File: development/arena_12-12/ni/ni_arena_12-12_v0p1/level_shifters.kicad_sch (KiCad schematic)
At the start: 15 parts, among them U1 TXB0108PW, U2 TXB0108PW, U3 TXB0108PW, U4 TXB0108PW, U5 TXB0108PW

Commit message: Further work on 12-12 ni arena.
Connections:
- net PAN3V.EXT_INT: now also U5.8 (A7); no longer U4.8 (A7)
- net PAN3V.RESET: now also U5.9 (A8); no longer U4.9 (A8)
- net PAN5V.EXT_INT: now also U5.13 (B7); no longer U4.13 (B7)
- net PAN5V.RESET: now also U5.12 (B8); no longer U4.12 (B8)
- net PAN3V.CS_00: now reaches U1.1 (A1)
- net PAN5V.CS_00: now reaches U1.20 (B1)
- net PAN3V.MOSI_09: now reaches U5.1 (A1)
- net PAN5V.MISO_11: now reaches U5.14 (B6)
- net PAN5V.MOSI_11: now reaches U5.15 (B5)
- net PAN5V.MISO_10: now reaches U5.16 (B4)
- net PAN5V.MOSI_10: now reaches U5.17 (B3)
- net PAN5V.MISO_09: now reaches U5.18 (B2)
- net PAN5V.MOSI_09: now reaches U5.20 (B1)
- net PAN3V.MISO_09: now reaches U5.3 (A2)
- net PAN3V.MOSI_10: now reaches U5.4 (A3)
- net PAN3V.MISO_10: now reaches U5.5 (A4)
- net PAN3V.MOSI_11: now reaches U5.6 (A5)
- net PAN3V.MISO_11: now reaches U5.7 (A6)
- net PAN3V.SCK_00: now reaches U2.1 (A1)
- net PAN5V.SCK_00: now reaches U2.20 (B1)
- net PAN3V.MOSI_01: now reaches U3.1 (A1)
- net PAN5V.MOSI_01: now reaches U3.20 (B1)
- net PAN3V.MOSI_05: now reaches U4.1 (A1)
- net PAN5V.MOSI_05: now reaches U4.20 (B1)
- net PAN3V.CS_0 renamed PAN3V.CS_01
- net PAN3V.CS_1 renamed PAN3V.CS_02
- net PAN3V.CS_2 renamed PAN3V.CS_03
- net PAN3V.CS_3 renamed PAN3V.CS_04
- net PAN3V.CS_4 renamed PAN3V.CS_05
- net PAN3V.CS_5 renamed PAN3V.CS_06
- net PAN3V.CS_6 renamed PAN3V.CS_07
- net PAN3V.CS_7 renamed PAN3V.SCK_01
- net PAN3V.MISO_0 renamed PAN3V.MOSI_02
- net PAN3V.MISO_1 renamed PAN3V.MOSI_03
- net PAN3V.MISO_2 renamed PAN3V.MOSI_04
- net PAN3V.MISO_3 renamed PAN3V.MISO_05
- net PAN3V.MISO_4 renamed PAN3V.MISO_06
- net PAN3V.MISO_5 renamed PAN3V.MISO_07
- net PAN3V.MOSI_0 renamed PAN3V.MISO_01
- net PAN3V.MOSI_1 renamed PAN3V.MISO_02
- net PAN3V.MOSI_2 renamed PAN3V.MISO_03
- net PAN3V.MOSI_3 renamed PAN3V.MISO_04
- net PAN3V.MOSI_4 renamed PAN3V.MOSI_06
- net PAN3V.MOSI_5 renamed PAN3V.MOSI_07
- net PAN3V.SCK_0 renamed PAN3V.SCK_02
- net PAN3V.SCK_1 renamed PAN3V.SCK_03
- net PAN3V.SCK_2 renamed PAN3V.SCK_04
- net PAN3V.SCK_3 renamed PAN3V.SCK_05
- net PAN3V.SCK_4 renamed PAN3V.MOSI_00
- net PAN3V.SCK_5 renamed PAN3V.MISO_00
- net PAN5V.CS_0 renamed PAN5V.CS_01
- net PAN5V.CS_1 renamed PAN5V.CS_02
- net PAN5V.CS_2 renamed PAN5V.CS_03
- net PAN5V.CS_3 renamed PAN5V.CS_04
- net PAN5V.CS_4 renamed PAN5V.CS_05
- net PAN5V.CS_5 renamed PAN5V.CS_06
- net PAN5V.CS_6 renamed PAN5V.CS_07
- net PAN5V.CS_7 renamed PAN5V.SCK_01
- net PAN5V.MISO_0 renamed PAN5V.MOSI_02
- net PAN5V.MISO_1 renamed PAN5V.MOSI_03
- net PAN5V.MISO_2 renamed PAN5V.MOSI_04
- net PAN5V.MISO_3 renamed PAN5V.MISO_05
- net PAN5V.MISO_4 renamed PAN5V.MISO_06
- net PAN5V.MISO_5 renamed PAN5V.MISO_07
- net PAN5V.MOSI_0 renamed PAN5V.MISO_01
- net PAN5V.MOSI_1 renamed PAN5V.MISO_02
- net PAN5V.MOSI_2 renamed PAN5V.MISO_03
- net PAN5V.MOSI_3 renamed PAN5V.MISO_04
- net PAN5V.MOSI_4 renamed PAN5V.MOSI_06
- net PAN5V.MOSI_5 renamed PAN5V.MOSI_07
- net PAN5V.SCK_0 renamed PAN5V.SCK_02
- net PAN5V.SCK_1 renamed PAN5V.SCK_03
- net PAN5V.SCK_2 renamed PAN5V.SCK_04
- net PAN5V.SCK_3 renamed PAN5V.SCK_05
- net PAN5V.SCK_4 renamed PAN5V.MOSI_00
- net PAN5V.SCK_5 renamed PAN5V.MISO_00
- new net PAN3V.MISO_08: U4.9 (A8)
- new net PAN3V.MOSI_08: U4.8 (A7)
- new net PAN5V.MISO_08: U4.12 (B8)
- new net PAN5V.MOSI_08: U4.13 (B7)
- no-connect marks 10 -> 0

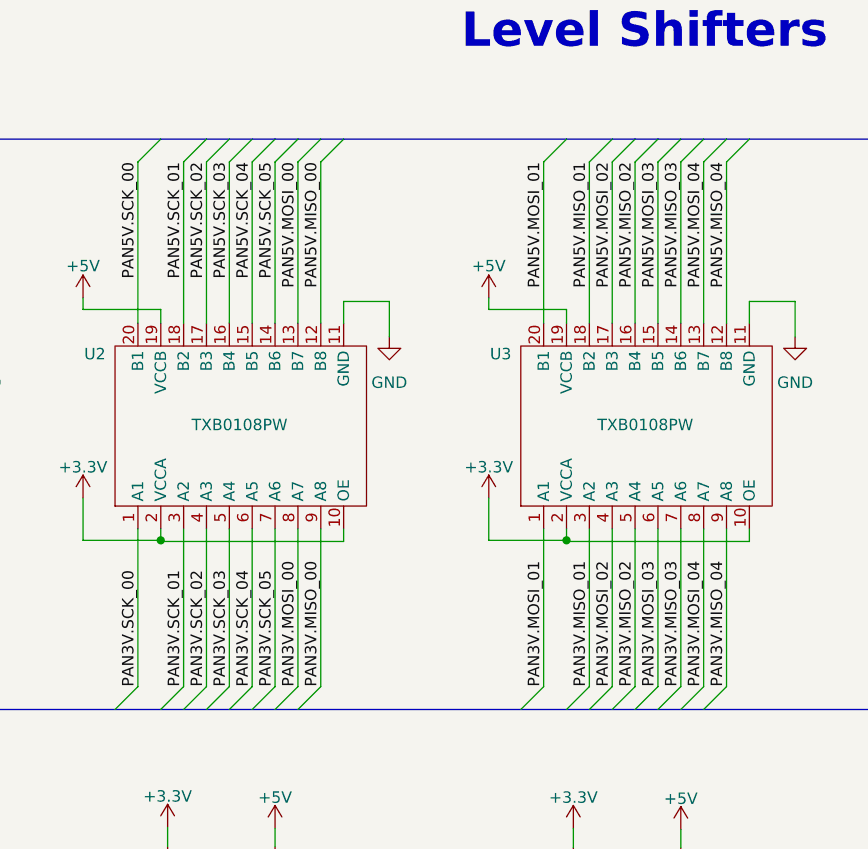
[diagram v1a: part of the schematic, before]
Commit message: Finished initial schematic and layout for 12-12 NI arena (without voltage regulators).
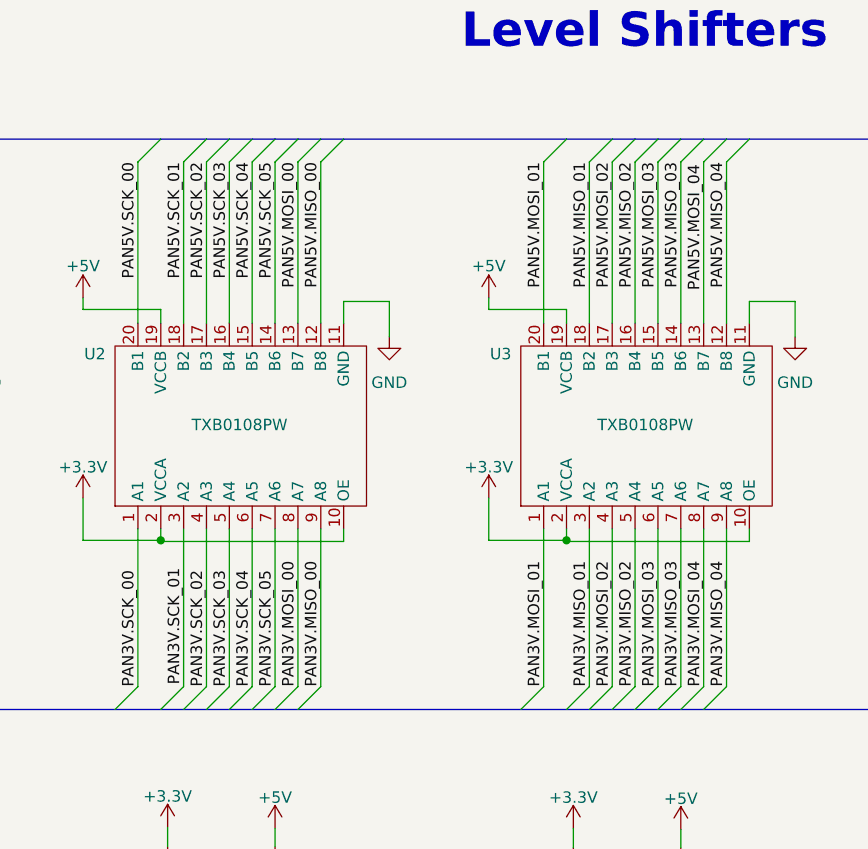
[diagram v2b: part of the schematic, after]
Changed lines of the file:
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@@
     (effects (font (size 1.27 1.27)) (justify left bottom))
   )
-  (label "PAN3V.SCK_01" (at 109.093 93.599 90) (fields_autoplaced)
+  (label "PAN3V.SCK_01" (at 109.093 93.345 90) (fields_autoplaced)
     (effects (font (size 1.27 1.27)) (justify left bottom))
   )
@@
     (effects (font (size 1.27 1.27)) (justify right bottom))
   )
-  (label "PAN5V.MOSI_04" (at 166.878 35.306 270) (fields_autoplaced)
+  (label "PAN5V.MOSI_04" (at 166.878 35.56 270) (fields_autoplaced)
     (effects (font (size 1.27 1.27)) (justify right bottom))
   )
